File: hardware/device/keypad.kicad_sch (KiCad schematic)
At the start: 66 parts, among them SW1 TRIG1, SW10 TRIG10, SW11 TRIG11, SW12 TRIG12, SW13 TRIG13, SW14 TRIG14, SW15 TRIG15, SW16 TRIG16, SW17 WHEEL_BTN, SW18 HELP, SW19 LEFT_BTN, SW2 TRIG2, SW20 RIGHT_BTN, SW3 TRIG3, SW4 TRIG4, SW5 TRIG5, SW6 TRIG6, SW7 TRIG7, SW8 TRIG8, SW9 TRIG9, U25 TCA8418RTWR

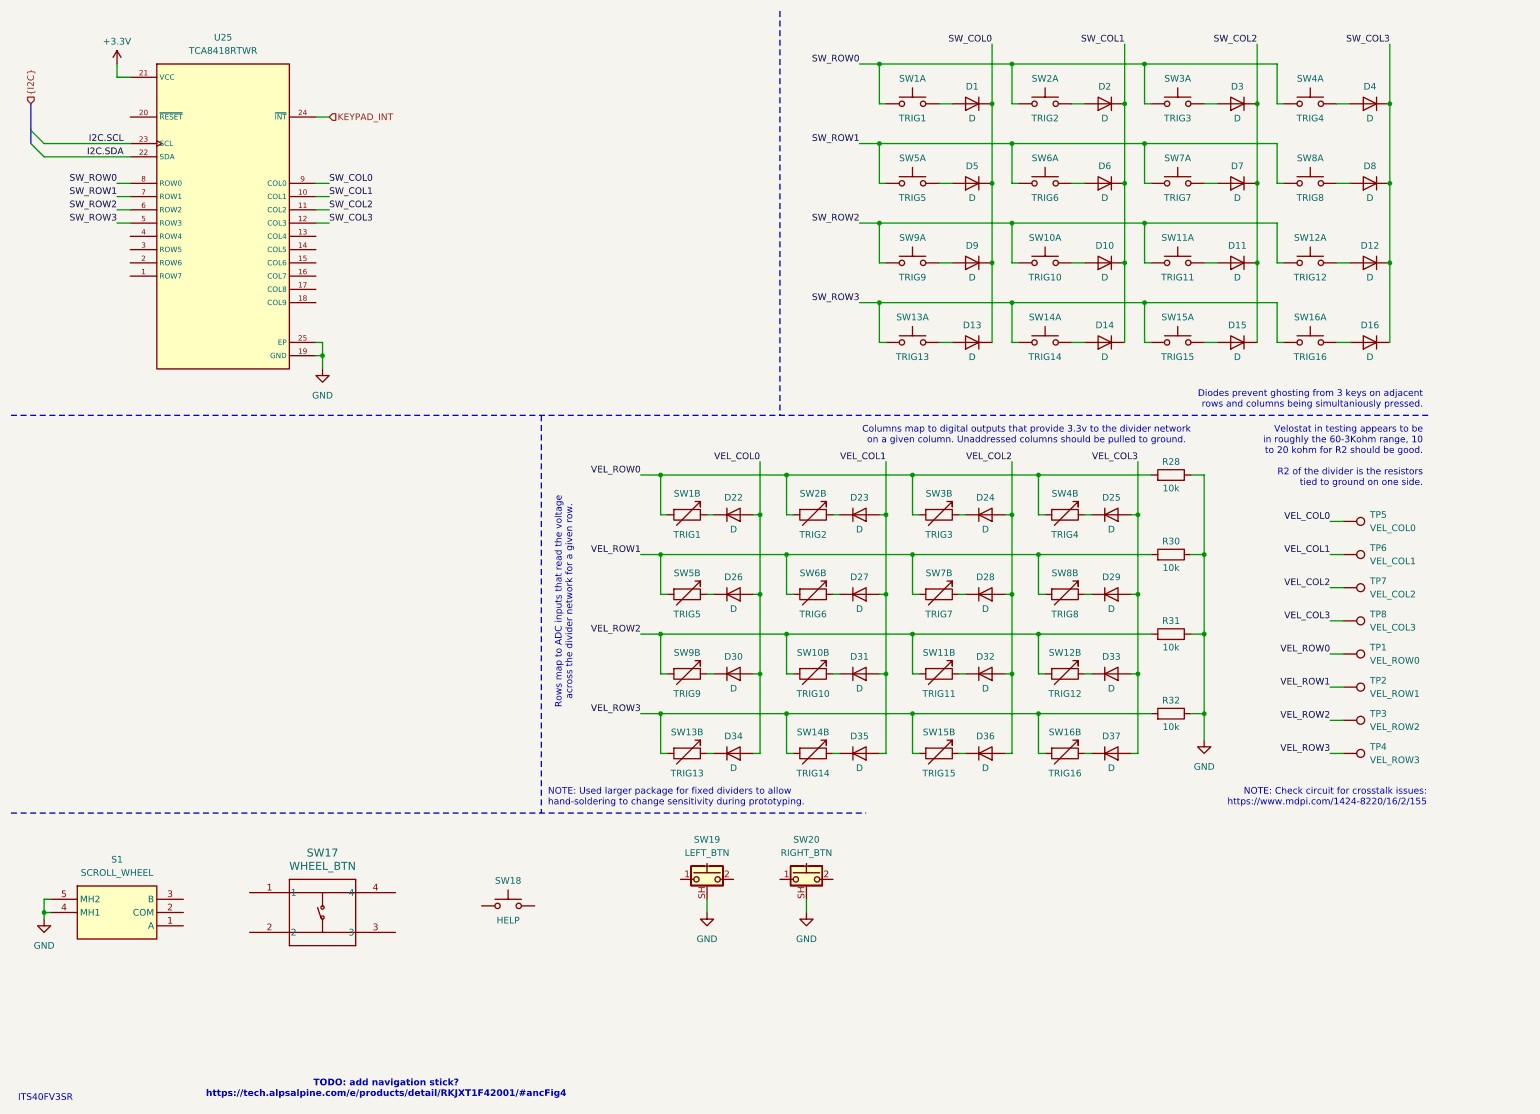
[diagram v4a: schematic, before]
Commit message: feat: keypad schematic cleanup
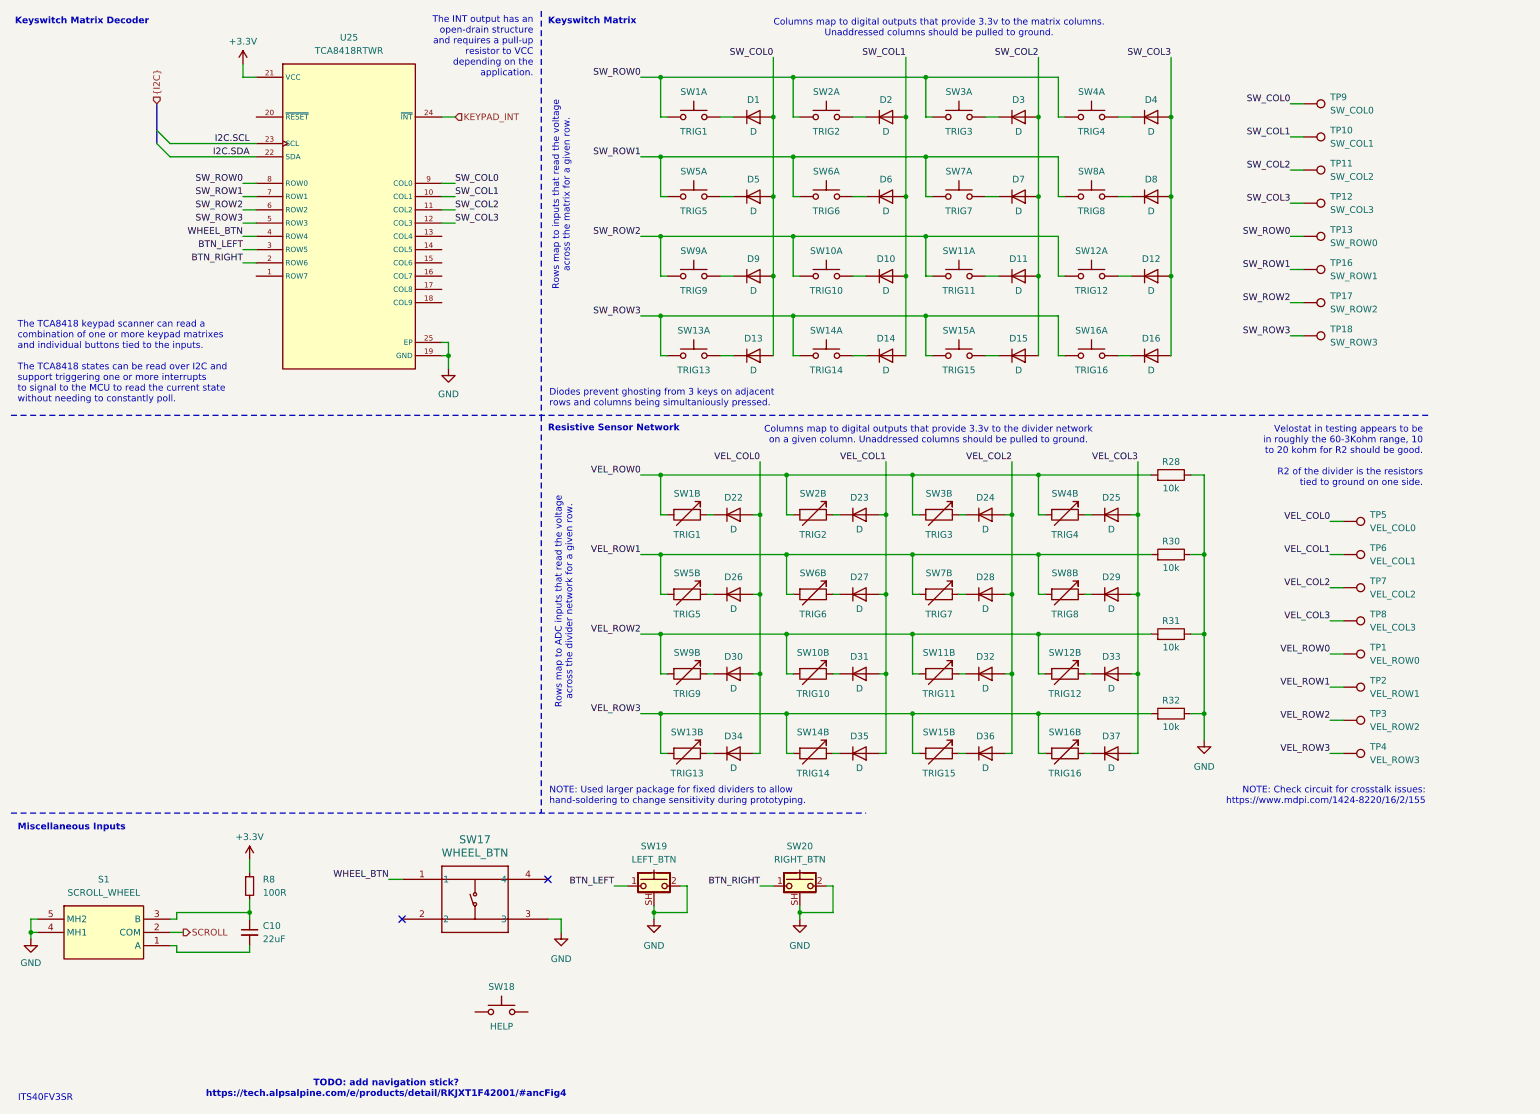
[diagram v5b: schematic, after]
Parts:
- added C10: 22uF, symbol Device:C_Small
- added R8: 100R, symbol Device:R_Small
- added TP10: SW_COL1, TestPoint:TestPoint_Pad_D2.5mm, symbol Connector:TestPoint
- added TP11: SW_COL2, TestPoint:TestPoint_Pad_D2.5mm, symbol Connector:TestPoint
- added TP12: SW_COL3, TestPoint:TestPoint_Pad_D2.5mm, symbol Connector:TestPoint
- added TP13: SW_ROW0, TestPoint:TestPoint_Pad_D2.5mm, symbol Connector:TestPoint
- added TP16: SW_ROW1, TestPoint:TestPoint_Pad_D2.5mm, symbol Connector:TestPoint
- added TP17: SW_ROW2, TestPoint:TestPoint_Pad_D2.5mm, symbol Connector:TestPoint
- added TP18: SW_ROW3, TestPoint:TestPoint_Pad_D2.5mm, symbol Connector:TestPoint
- added TP9: SW_COL0, TestPoint:TestPoint_Pad_D2.5mm, symbol Connector:TestPoint
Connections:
- net +3.3V: now also R8.1
- net GND: now also SW17.3, SW19.2, SW20.2
- net SW_COL0: now also D1.2 (A), D13.2 (A), D5.2 (A), D9.2 (A), TP9.1; no longer D1.1 (K), D13.1 (K), D5.1 (K), D9.1 (K)
- net SW_COL1: now also D10.2 (A), D14.2 (A), D2.2 (A), D6.2 (A), TP10.1; no longer D10.1 (K), D14.1 (K), D2.1 (K), D6.1 (K)
- net SW_COL2: now also D11.2 (A), D15.2 (A), D3.2 (A), D7.2 (A), TP11.1; no longer D11.1 (K), D15.1 (K), D3.1 (K), D7.1 (K)
- net SW_COL3: now also D12.2 (A), D16.2 (A), D4.2 (A), D8.2 (A), TP12.1; no longer D12.1 (K), D16.1 (K), D4.1 (K), D8.1 (K)
- net SW_ROW0: now also TP13.1
- net SW_ROW1: now also TP16.1
- net SW_ROW2: now also TP17.1
- net SW_ROW3: now also TP18.1
- net at SW2.2: now also D2.1 (K); no longer D2.2 (A)
- net BTN_LEFT: now reaches SW19.1
- net BTN_LEFT: now also U25.3 (ROW5)
- net at SW7.2: now also D7.1 (K); no longer D7.2 (A)
- net at SW6.2: now also D6.1 (K); no longer D6.2 (A)
- net at S1.1 (A): now also C10.2
- net SCROLL: now reaches S1.2 (COM)
- net at S1.3 (B): now also C10.1, R8.2
- net BTN_RIGHT: now reaches SW20.1
- net BTN_RIGHT: now also U25.2 (ROW6)
- net WHEEL_BTN: now reaches U25.4 (ROW4)
- net WHEEL_BTN: now also SW17.1
- net at SW12.2: now also D12.1 (K); no longer D12.2 (A)
- net at SW1.2: now also D1.1 (K); no longer D1.2 (A)
- net at SW13.2: now also D13.1 (K); no longer D13.2 (A)
- net at SW11.2: now also D11.1 (K); no longer D11.2 (A)
- net at SW4.2: now also D4.1 (K); no longer D4.2 (A)
- net at SW15.2: now also D15.1 (K); no longer D15.2 (A)
- net at SW14.2: now also D14.1 (K); no longer D14.2 (A)
- net at SW16.2: now also D16.1 (K); no longer D16.2 (A)
- net at SW8.2: now also D8.1 (K); no longer D8.2 (A)
- net at SW3.2: now also D3.1 (K); no longer D3.2 (A)
- net at SW9.2: now also D9.1 (K); no longer D9.2 (A)
- net at SW5.2: now also D5.1 (K); no longer D5.2 (A)
- net at SW10.2: now also D10.1 (K); no longer D10.2 (A)
- no-connect marks 0 -> 2
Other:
- note added: "Columns map to digital outputs that provide 3.3v to the matrix columns. Unaddressed columns should be pulled to ground."
- note added: "Keyswitch Matrix"
- note added: "Keyswitch Matrix Decoder"
- note added: "Miscellaneous Inputs"
- note added: "Resistive Sensor Network"
- note added: "Rows map to inputs that read the voltage across the matrix for a given row."
- note added: "The INT output has an open-drain structure and requires a pull-up resistor to VCC depending on the application."
- note added: "The TCA8418 keypad scanner can read a combination of one or more keypad matrixes and individual buttons tied to the inputs. The TCA8418 states can be read over I2C and support triggering one or more interrupts to signal to the MCU to read the current state without needing to constantly poll."
- moved on the sheet: D1, D10, D11, D12, D13, D14, D15, D16, D2, D3, D4, D5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

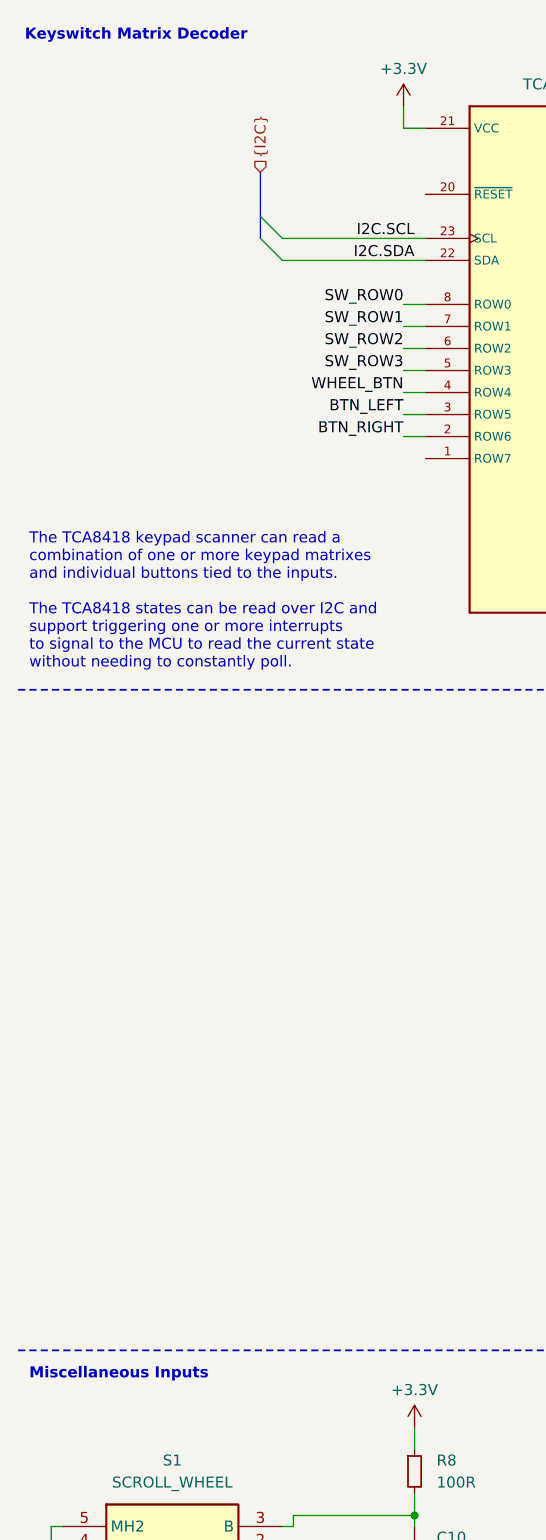
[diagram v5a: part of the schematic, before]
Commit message: feat: add buffer for LED logic level conversion
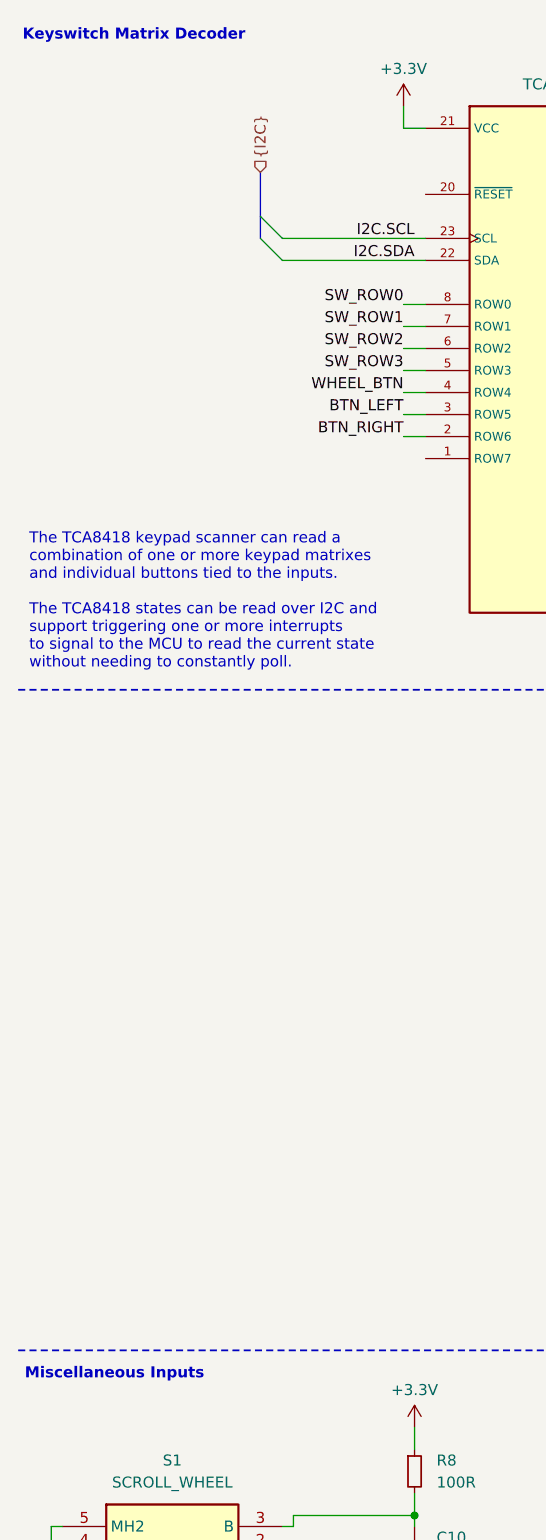
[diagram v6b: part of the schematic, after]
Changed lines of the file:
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@@
 	(text "Miscellaneous Inputs"
 		(exclude_from_sim no)
-		(at 13.97 168.402 0)
+		(at 13.462 168.402 0)
 		(effects
 			(font
@@
 	(text "Keyswitch Matrix Decoder"
 		(exclude_from_sim no)
-		(at 13.462 13.97 0)
+		(at 13.208 13.97 0)
 		(effects
 			(font

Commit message: chore: schematic organization
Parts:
- C10: footprint (none) -> Capacitor_SMD:C_0402_1005Metric
- R8: footprint (none) -> Resistor_SMD:R_0402_1005Metric
- TP1, TP10, TP11, TP12, TP13, TP16, TP17, TP18, TP2, TP3, TP4, TP5, TP6, TP7, TP8, TP9: footprint TestPoint:TestPoint_Pad_D2.5mm -> TestPoint:TestPoint_Pad_D1.5mm
- U25: JLC (none) -> C138713
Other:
- note added: "NOTE: Check circuit for crosstalk issues https://www.mdpi.com/1424-8220/16/2/155"
- note added: "Row/Column Anti-ghosting Keyswitch Matrix"
- note added: "Used hand-solder package for to change sensitivity during prototyping."
- note added: "Velocity and After-Touch Reistive Sensor Network"
- note removed: "NOTE: Check circuit for crosstalk issues: https://www.mdpi.com/1424-8220/16/2/155"
- note removed: "NOTE: Used larger package for fixed dividers to allow hand-soldering to change sensitivity during prototyping."
- moved on the sheet: D1, D10, D11, D12, D13, D14, D15, D16, D2, D22, D23, D24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

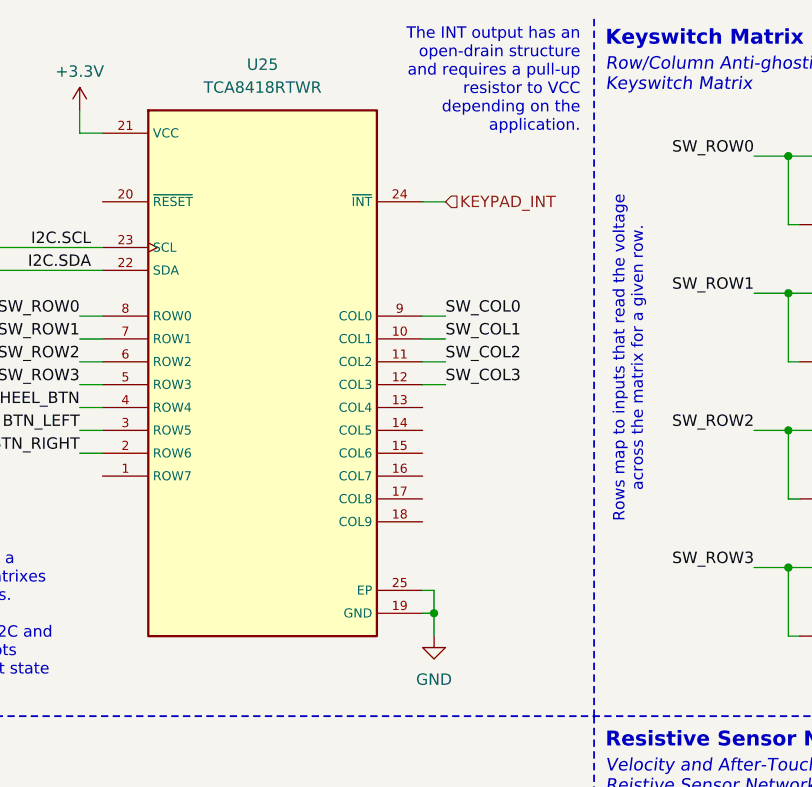
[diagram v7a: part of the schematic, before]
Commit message: feat: add plated mounting holes
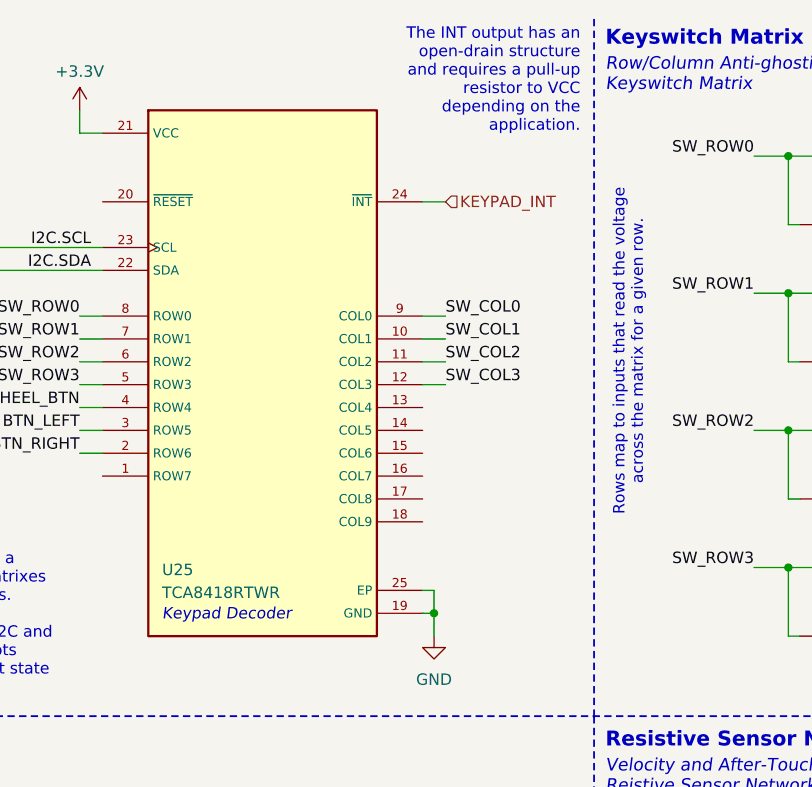
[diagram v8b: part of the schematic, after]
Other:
- note added: "Keypad Decoder"
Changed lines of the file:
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@@
 		)
 	)
+	(text "Keypad Decoder"
+		(exclude_from_sim no)
+		(at 66.294 78.232 0)
+		(effects
+			(font
+				(size 1.27 1.27)
+				(thickness 0.1588)
+				(italic yes)
+				(color 132 132 132 1)
+			)
+			(justify left top)
+		)
+	)
 	(text "Keyswitch Matrix Decoder"
 		(exclude_from_sim no)
@@
 	(text "Rows map to inputs that read the voltage\nacross the matrix for a given row."
 		(exclude_from_sim no)
-		(at 118.11 50.546 90)
+		(at 118.11 49.784 90)
 		(effects
 			(font
@@
 		(on_board yes)
 		(dnp no)
-		(fields_autoplaced yes)
 		(property "Reference" "U25"
-			(at 77.47 17.78 0)
+			(at 66.294 73.914 0)
 			(effects
 				(font
 					(size 1.27 1.27)
 				)
+				(justify left)
 			)
 		)
 		(property "Value" "TCA8418RTWR"
-			(at 77.47 20.32 0)
+			(at 66.294 76.454 0)
 			(effects
 				(font
 					(size 1.27 1.27)
 				)
+				(justify left)
 			)
 		)
